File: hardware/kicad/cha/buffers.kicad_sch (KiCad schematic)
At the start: 26 parts, among them U10 74AHCT1G32, U11 74LVC1G07, U3 74LVC16244A, U4 74LVC16244A, U5 74LVC16244A, U6 74LVC16244A, U7 74AHCT16244, U8 74AHCT16244, U9 74AHCT244

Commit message: Circuits imprimés 2 couches : placement et affectation des broches FPGA
- hardware/gen/pcb.py : empreintes et réseaux depuis boards.py, contour
  depuis outline.py ; ancres placées (contacts, rangée de tampons, FPGA,
  mémoires ; CHA : Pico au centre, microSD et bouton en haut), passifs
  au plus près de leur broche, masse coulée sur les deux faces.
- --pins : signaux des FPGA affectés aux broches tournées vers leur
  cible en conservant l'ordre circulaire (pins_opt.json, repris par
  fpga_pins.py) ; stable en trois passes.
- boards.py : canaux des tampons triés selon la position des contacts.
- hardware/gen/route.py : export Specctra, Freerouting, relecture de la
  session, DRC.
Placement-routage FPGA avec les nouvelles broches : en cours de
vérification.

Co-Authored-By: Claude Opus 5.5 <noreply@anthropic.com>
Claude-Session: https://claude.ai/code/session_01WKfXP1YJ8otGxZ5dsY6Agh
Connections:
- net 12M: now also U6.2 (1Y1); no longer U4.19 (4Y1)
- net 2H1: now also U5.23 (4Y4); no longer U4.17 (3Y4)
- net AES_12M: now also U6.47 (1A1); no longer U4.30 (4A1)
- net AES_2H1: now also U5.26 (4A4); no longer U4.32 (3A4)
- net AES_CA4: now also U5.32 (3A4); no longer U4.33 (3A3)
- net AES_DOTA: now also U7.14 (3Y2); no longer U7.13 (3Y1)
- net AES_DOTB: now also U7.13 (3Y1); no longer U7.14 (3Y2)
- net AES_EVEN: now also U5.27 (4A3); no longer U4.29 (4A2)
- net AES_FIXD0: now also U8.3 (1Y2); no longer U7.16 (3Y3)
- net AES_FIXD1: now also U8.2 (1Y1); no longer U7.17 (3Y4)
- net AES_FIXD2: now also U7.23 (4Y4); no longer U7.19 (4Y1)
- net AES_FIXD3: now also U7.22 (4Y3); no longer U7.20 (4Y2)
- net AES_FIXD4: now also U7.20 (4Y2); no longer U7.22 (4Y3)
- net AES_FIXD5: now also U7.19 (4Y1); no longer U7.23 (4Y4)
- net AES_FIXD6: now also U7.17 (3Y4); no longer U8.2 (1Y1)
- net AES_FIXD7: now also U7.16 (3Y3); no longer U8.3 (1Y2)
- net AES_GAD0: now also U7.12 (2Y4); no longer U7.2 (1Y1)
- net AES_GAD1: now also U7.11 (2Y3); no longer U7.3 (1Y2)
- net AES_GAD2: now also U7.9 (2Y2); no longer U7.5 (1Y3)
- net AES_GAD3: now also U7.8 (2Y1); no longer U7.6 (1Y4)
- net AES_GBD0: now also U7.6 (1Y4); no longer U7.8 (2Y1)
- net AES_GBD1: now also U7.5 (1Y3); no longer U7.9 (2Y2)
- net AES_GBD2: now also U7.3 (1Y2); no longer U7.11 (2Y3)
- net AES_GBD3: now also U7.2 (1Y1); no longer U7.12 (2Y4)
- net AES_H: now also U5.29 (4A2); no longer U4.26 (4A4)
- net AES_LOAD: now also U5.30 (4A1); no longer U4.27 (4A3)
- net AES_P0: now also U5.35 (3A2); no longer U3.47 (1A1)
- net AES_P1: now also U5.33 (3A3); no longer U3.46 (1A2)
- net AES_P10: now also U4.26 (4A4); no longer U3.33 (3A3)
- net AES_P11: now also U5.47 (1A1); no longer U3.32 (3A4)
- net AES_P12: now also U4.29 (4A2); no longer U3.30 (4A1)
- net AES_P13: now also U4.27 (4A3); no longer U3.29 (4A2)
- net AES_P14: now also U4.32 (3A4); no longer U3.27 (4A3)
- net AES_P15: now also U4.30 (4A1); no longer U3.26 (4A4)
- net AES_P16: now also U4.35 (3A2); no longer U4.47 (1A1)
- net AES_P17: now also U4.33 (3A3); no longer U4.46 (1A2)
- net AES_P18: now also U4.37 (2A4); no longer U4.44 (1A3)
- net AES_P19: now also U4.36 (3A1); no longer U4.43 (1A4)
- net AES_P2: now also U5.37 (2A4); no longer U3.44 (1A3)
- net AES_P20: now also U4.40 (2A2); no longer U4.41 (2A1)
- net AES_P21: now also U4.38 (2A3); no longer U4.40 (2A2)
- net AES_P22: now also U4.43 (1A4); no longer U4.38 (2A3)
- net AES_P23: now also U4.41 (2A1); no longer U4.37 (2A4)
- net AES_P3: now also U5.36 (3A1); no longer U3.43 (1A4)
- net AES_P4: now also U5.40 (2A2); no longer U3.41 (2A1)
- net AES_P5: now also U5.38 (2A3); no longer U3.40 (2A2)
- net AES_P6: now also U5.43 (1A4); no longer U3.38 (2A3)
- net AES_P7: now also U5.41 (2A1); no longer U3.37 (2A4)
- net AES_P8: now also U5.46 (1A2); no longer U3.36 (3A1)
- net AES_P9: now also U5.44 (1A3); no longer U3.35 (3A2)
- net AES_PCK1B: now also U6.44 (1A3); no longer U4.36 (3A1)
- net AES_PCK2B: now also U6.46 (1A2); no longer U4.35 (3A2)
- net AES_SDA0: now also U4.46 (1A2); no longer U5.47 (1A1)
- net AES_SDA1: now also U4.47 (1A1); no longer U5.46 (1A2)
- net AES_SDA10: now also U3.37 (2A4); no longer U5.33 (3A3)
- net AES_SDA11: now also U3.38 (2A3); no longer U5.32 (3A4)
- net AES_SDA12: now also U3.40 (2A2); no longer U5.30 (4A1)
- net AES_SDA13: now also U3.41 (2A1); no longer U5.29 (4A2)
- net AES_SDA14: now also U3.43 (1A4); no longer U5.27 (4A3)
- net AES_SDA15: now also U3.44 (1A3); no longer U5.26 (4A4)
- net AES_SDA2: now also U3.26 (4A4); no longer U5.44 (1A3)
- net AES_SDA3: now also U3.27 (4A3); no longer U5.43 (1A4)
- net AES_SDA4: now also U3.29 (4A2); no longer U5.41 (2A1)
- net AES_SDA5: now also U3.30 (4A1); no longer U5.40 (2A2)
- net AES_SDA6: now also U3.32 (3A4); no longer U5.38 (2A3)
- net AES_SDA7: now also U3.33 (3A3); no longer U5.37 (2A4)
- net AES_SDA8: now also U3.35 (3A2); no longer U5.36 (3A1)
- net AES_SDA9: now also U3.36 (3A1); no longer U5.35 (3A2)
- net AES_SDMRD: now also U3.46 (1A2); no longer U6.47 (1A1)
- net AES_SDRD0: now also U4.44 (1A3); no longer U6.44 (1A3)
- net AES_SDROM: now also U3.47 (1A1); no longer U6.46 (1A2)
- net CA4: now also U5.17 (3Y4); no longer U4.16 (3Y3)
- net DOTA: now also U7.35 (3A2); no longer U7.36 (3A1)
- net DOTB: now also U7.36 (3A1); no longer U7.35 (3A2)
- net EVEN: now also U5.22 (4Y3); no longer U4.20 (4Y2)
- net FIXD0: now also U8.46 (1A2); no longer U7.33 (3A3)
- net FIXD1: now also U8.47 (1A1); no longer U7.32 (3A4)
- net FIXD2: now also U7.26 (4A4); no longer U7.30 (4A1)
- net FIXD3: now also U7.27 (4A3); no longer U7.29 (4A2)
- net FIXD4: now also U7.29 (4A2); no longer U7.27 (4A3)
- net FIXD5: now also U7.30 (4A1); no longer U7.26 (4A4)
- net FIXD6: now also U7.32 (3A4); no longer U8.47 (1A1)
- net FIXD7: now also U7.33 (3A3); no longer U8.46 (1A2)
- net GAD0: now also U7.37 (2A4); no longer U7.47 (1A1)
- net GAD1: now also U7.38 (2A3); no longer U7.46 (1A2)
- net GAD2: now also U7.40 (2A2); no longer U7.44 (1A3)
- net GAD3: now also U7.41 (2A1); no longer U7.43 (1A4)
- net GBD0: now also U7.43 (1A4); no longer U7.41 (2A1)
- net GBD1: now also U7.44 (1A3); no longer U7.40 (2A2)
- net GBD2: now also U7.46 (1A2); no longer U7.38 (2A3)
- net GBD3: now also U7.47 (1A1); no longer U7.37 (2A4)
- net H: now also U5.20 (4Y2); no longer U4.23 (4Y4)
- net LOAD: now also U5.19 (4Y1); no longer U4.22 (4Y3)
- net P0: now also U5.14 (3Y2); no longer U3.2 (1Y1)
- net P1: now also U5.16 (3Y3); no longer U3.3 (1Y2)
- net P10: now also U4.23 (4Y4); no longer U3.16 (3Y3)
- net P11: now also U5.2 (1Y1); no longer U3.17 (3Y4)
- net P12: now also U4.20 (4Y2); no longer U3.19 (4Y1)
- net P13: now also U4.22 (4Y3); no longer U3.20 (4Y2)
- net P14: now also U4.17 (3Y4); no longer U3.22 (4Y3)
- net P15: now also U4.19 (4Y1); no longer U3.23 (4Y4)
- net P16: now also U4.14 (3Y2); no longer U4.2 (1Y1)
- net P17: now also U4.16 (3Y3); no longer U4.3 (1Y2)
- net P18: now also U4.12 (2Y4); no longer U4.5 (1Y3)
- net P19: now also U4.13 (3Y1); no longer U4.6 (1Y4)
- net P2: now also U5.12 (2Y4); no longer U3.5 (1Y3)
- net P20: now also U4.9 (2Y2); no longer U4.8 (2Y1)
- net P21: now also U4.11 (2Y3); no longer U4.9 (2Y2)
- net P22: now also U4.6 (1Y4); no longer U4.11 (2Y3)
- net P23: now also U4.8 (2Y1); no longer U4.12 (2Y4)
- net P3: now also U5.13 (3Y1); no longer U3.6 (1Y4)
- net P4: now also U5.9 (2Y2); no longer U3.8 (2Y1)
- net P5: now also U5.11 (2Y3); no longer U3.9 (2Y2)
- net P6: now also U5.6 (1Y4); no longer U3.11 (2Y3)
- net P7: now also U5.8 (2Y1); no longer U3.12 (2Y4)
- net P8: now also U5.3 (1Y2); no longer U3.13 (3Y1)
- net P9: now also U5.5 (1Y3); no longer U3.14 (3Y2)
- net PCK1B: now also U6.5 (1Y3); no longer U4.13 (3Y1)
- net PCK2B: now also U6.3 (1Y2); no longer U4.14 (3Y2)
- net SDA0: now also U4.3 (1Y2); no longer U5.2 (1Y1)
- net SDA1: now also U4.2 (1Y1); no longer U5.3 (1Y2)
- net SDA10: now also U3.12 (2Y4); no longer U5.16 (3Y3)
- net SDA11: now also U3.11 (2Y3); no longer U5.17 (3Y4)
- net SDA12: now also U3.9 (2Y2); no longer U5.19 (4Y1)
- net SDA13: now also U3.8 (2Y1); no longer U5.20 (4Y2)
- net SDA14: now also U3.6 (1Y4); no longer U5.22 (4Y3)
- net SDA15: now also U3.5 (1Y3); no longer U5.23 (4Y4)
- net SDA2: now also U3.23 (4Y4); no longer U5.5 (1Y3)
- net SDA3: now also U3.22 (4Y3); no longer U5.6 (1Y4)
- net SDA4: now also U3.20 (4Y2); no longer U5.8 (2Y1)
- net SDA5: now also U3.19 (4Y1); no longer U5.9 (2Y2)
- net SDA6: now also U3.17 (3Y4); no longer U5.11 (2Y3)
- net SDA7: now also U3.16 (3Y3); no longer U5.12 (2Y4)
- net SDA8: now also U3.14 (3Y2); no longer U5.13 (3Y1)
- net SDA9: now also U3.13 (3Y1); no longer U5.14 (3Y2)
- net SDMRD_N: now also U3.3 (1Y2); no longer U6.2 (1Y1)
- net SDRD0_N: now also U4.5 (1Y3); no longer U6.5 (1Y3)
- net SDROM_N: now also U3.2 (1Y1); no longer U6.3 (1Y2)

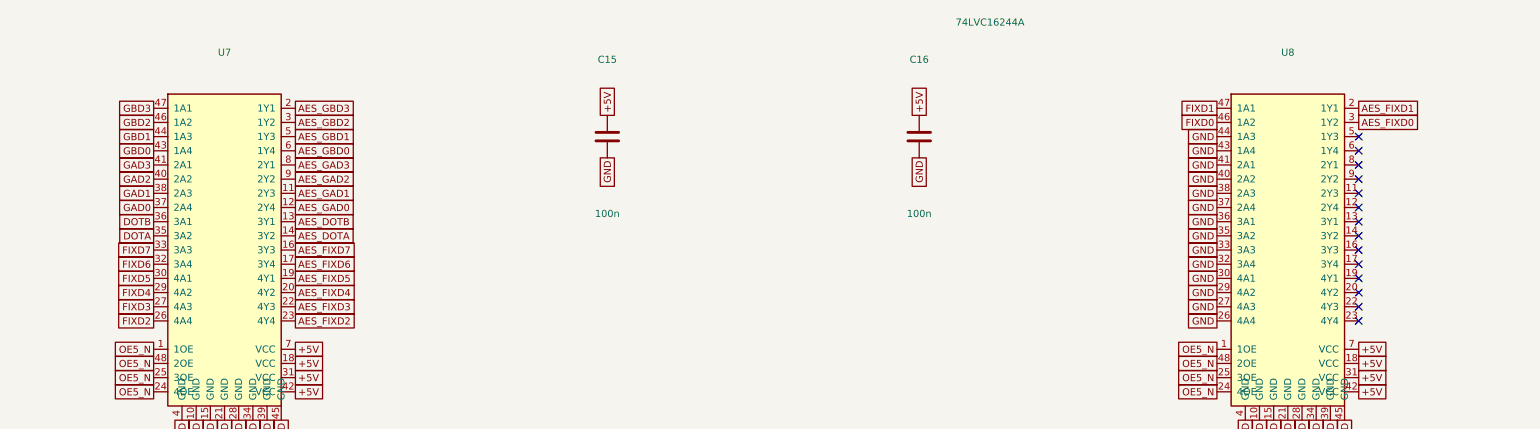
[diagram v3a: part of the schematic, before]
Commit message: CHA : canaux du tampon de sortie U7 groupés par FPGA source
Couche fixe (FPGA SM) puis sprites (FPGA C), chaque groupe dans l'ordre
des contacts : les deux groupes ne se croisent plus le long de la
rangée d'entrée du tampon, où les pistes FIXD enfermaient DOTA et GAD0.
Broches des FPGA C et SM réoptimisées, carte CHA régénérée (contrôle
Freerouting sans violation) ; nouveau routage en cours.

Co-Authored-By: Claude Opus 5.5 <noreply@anthropic.com>
Claude-Session: https://claude.ai/code/session_01WKfXP1YJ8otGxZ5dsY6Agh
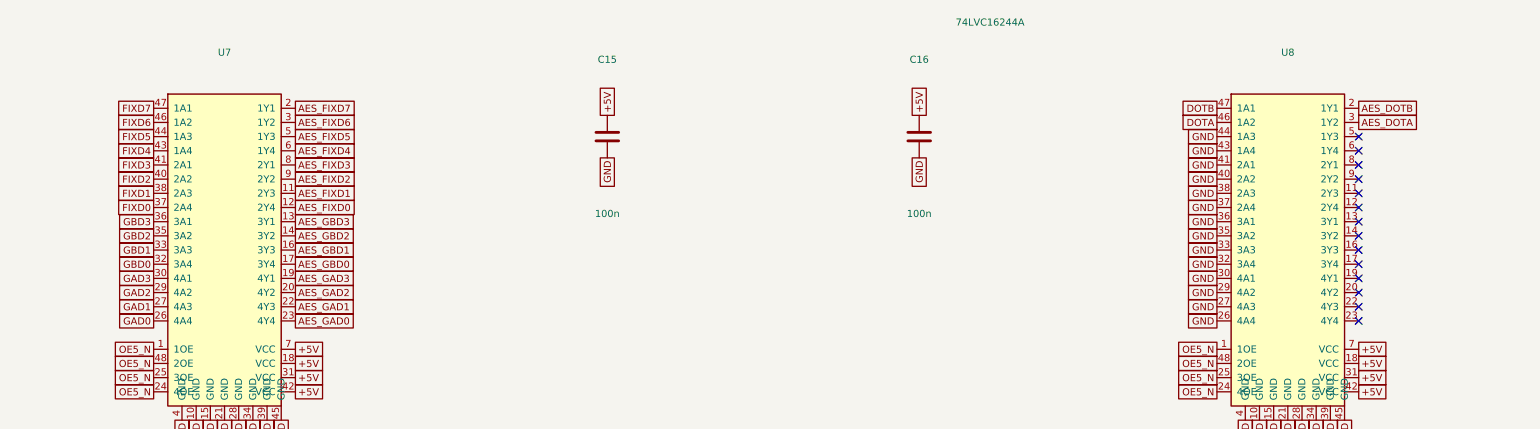
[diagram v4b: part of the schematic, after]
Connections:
- net AES_DOTA: now also U8.3 (1Y2); no longer U7.14 (3Y2)
- net AES_DOTB: now also U8.2 (1Y1); no longer U7.13 (3Y1)
- net AES_FIXD0: now also U7.12 (2Y4); no longer U8.3 (1Y2)
- net AES_FIXD1: now also U7.11 (2Y3); no longer U8.2 (1Y1)
- net AES_FIXD2: now also U7.9 (2Y2); no longer U7.23 (4Y4)
- net AES_FIXD3: now also U7.8 (2Y1); no longer U7.22 (4Y3)
- net AES_FIXD4: now also U7.6 (1Y4); no longer U7.20 (4Y2)
- net AES_FIXD5: now also U7.5 (1Y3); no longer U7.19 (4Y1)
- net AES_FIXD6: now also U7.3 (1Y2); no longer U7.17 (3Y4)
- net AES_FIXD7: now also U7.2 (1Y1); no longer U7.16 (3Y3)
- net AES_GAD0: now also U7.23 (4Y4); no longer U7.12 (2Y4)
- net AES_GAD1: now also U7.22 (4Y3); no longer U7.11 (2Y3)
- net AES_GAD2: now also U7.20 (4Y2); no longer U7.9 (2Y2)
- net AES_GAD3: now also U7.19 (4Y1); no longer U7.8 (2Y1)
- net AES_GBD0: now also U7.17 (3Y4); no longer U7.6 (1Y4)
- net AES_GBD1: now also U7.16 (3Y3); no longer U7.5 (1Y3)
- net AES_GBD2: now also U7.14 (3Y2); no longer U7.3 (1Y2)
- net AES_GBD3: now also U7.13 (3Y1); no longer U7.2 (1Y1)
- net DOTA: now also U8.46 (1A2); no longer U7.35 (3A2)
- net DOTB: now also U8.47 (1A1); no longer U7.36 (3A1)
- net FIXD0: now also U7.37 (2A4); no longer U8.46 (1A2)
- net FIXD1: now also U7.38 (2A3); no longer U8.47 (1A1)
- net FIXD2: now also U7.40 (2A2); no longer U7.26 (4A4)
- net FIXD3: now also U7.41 (2A1); no longer U7.27 (4A3)
- net FIXD4: now also U7.43 (1A4); no longer U7.29 (4A2)
- net FIXD5: now also U7.44 (1A3); no longer U7.30 (4A1)
- net FIXD6: now also U7.46 (1A2); no longer U7.32 (3A4)
- net FIXD7: now also U7.47 (1A1); no longer U7.33 (3A3)
- net GAD0: now also U7.26 (4A4); no longer U7.37 (2A4)
- net GAD1: now also U7.27 (4A3); no longer U7.38 (2A3)
- net GAD2: now also U7.29 (4A2); no longer U7.40 (2A2)
- net GAD3: now also U7.30 (4A1); no longer U7.41 (2A1)
- net GBD0: now also U7.32 (3A4); no longer U7.43 (1A4)
- net GBD1: now also U7.33 (3A3); no longer U7.44 (1A3)
- net GBD2: now also U7.35 (3A2); no longer U7.46 (1A2)
- net GBD3: now also U7.36 (3A1); no longer U7.47 (1A1)

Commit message: Régulateur 3,3 V à découpage, horloge SDRAM adaptée côté FPGA, U8 en 74AHCT125
- AP63203 (TSOT-23-6, sortie fixe 3,3 V, ~90 %) à la place de
  l'AMS1117 : ~0,15 W de pertes au lieu de ~0,75 W et moins de courant
  tiré sur le 5 V de la console ; L 4,7 µH, Cin 10 µF, Cout 2 x 22 µF.
- Résistance série de 33 ohms de l'horloge SDRAM déclarée avec le FPGA :
  placée à 2,7 mm de sa broche (au lieu de ~30 mm, côté SDRAM).
- CHA : U8 (16244 pour 2 canaux) remplacé par un 74AHCT125.
Cartes replacées, contrôle Freerouting sans violation ; routage des
deux cartes et vérification de timing en cours.

Co-Authored-By: Claude Opus 5.5 <noreply@anthropic.com>
Claude-Session: https://claude.ai/code/session_01WKfXP1YJ8otGxZ5dsY6Agh
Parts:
- removed C7, C8: 100n, Capacitor_SMD:C_0603_1608Metric, symbol Device:C
- removed U8: 74AHCT16244, Package_SO:TSSOP-48_6.1x12.5mm_P0.5mm, symbol SDAES:x16244
- added C22: 100n, Capacitor_SMD:C_0603_1608Metric, symbol Device:C
- added U8: 74AHCT125, Package_SO:TSSOP-14_4.4x5mm_P0.65mm, symbol 74xx:74LS125
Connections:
- net +3V3: now also C15.1, C16.1, C22.1; no longer C21.1
- net +5V: now also C21.1, U8.10, U8.13, U8.14 (VCC); no longer C15.1, C16.1
- net AES_DOTA: now also U8.6
- net AES_DOTB: now also U8.3
- net DOTA: now also U8.5
- net DOTB: now also U8.2
- net GND: now also C22.2, U8.12, U8.7 (GND), U8.9
- net OE5_N: now also U8.1, U8.4
- no-connect marks 28 -> 16

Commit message: CHA : canaux des tampons d'entrée groupés par FPGA de destination
SM seul (bus Z80, PCK2B, 2H1) à gauche, bus P0-P15 au milieu, C seul à
droite, chaque groupe dans l'ordre des contacts : le faisceau SDA entre
le FPGA SM et U3 ne se croise plus avec les signaux du FPGA C (SDA4
restait non routable). Carte CHA replacée, broches réoptimisées,
contrôle Freerouting sans violation ; routage en cours.

Co-Authored-By: Claude Opus 5.5 <noreply@anthropic.com>
Claude-Session: https://claude.ai/code/session_01WKfXP1YJ8otGxZ5dsY6Agh
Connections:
- net 12M: now also U6.3 (1Y2); no longer U6.2 (1Y1)
- net 2H1: now also U4.6 (1Y4); no longer U5.23 (4Y4)
- net AES_12M: now also U6.46 (1A2); no longer U6.47 (1A1)
- net AES_2H1: now also U4.43 (1A4); no longer U5.26 (4A4)
- net AES_CA4: now also U5.29 (4A2); no longer U5.32 (3A4)
- net AES_EVEN: now also U6.47 (1A1); no longer U5.27 (4A3)
- net AES_H: now also U5.26 (4A4); no longer U5.29 (4A2)
- net AES_LOAD: now also U5.27 (4A3); no longer U5.30 (4A1)
- net AES_P0: now also U5.43 (1A4); no longer U5.35 (3A2)
- net AES_P1: now also U5.41 (2A1); no longer U5.33 (3A3)
- net AES_P10: now also U4.35 (3A2); no longer U4.26 (4A4)
- net AES_P11: now also U4.33 (3A3); no longer U5.47 (1A1)
- net AES_P12: now also U4.37 (2A4); no longer U4.29 (4A2)
- net AES_P13: now also U4.36 (3A1); no longer U4.27 (4A3)
- net AES_P14: now also U4.40 (2A2); no longer U4.32 (3A4)
- net AES_P15: now also U4.38 (2A3); no longer U4.30 (4A1)
- net AES_P16: now also U5.32 (3A4); no longer U4.35 (3A2)
- net AES_P17: now also U5.30 (4A1); no longer U4.33 (3A3)
- net AES_P18: now also U5.35 (3A2); no longer U4.37 (2A4)
- net AES_P19: now also U5.33 (3A3); no longer U4.36 (3A1)
- net AES_P2: now also U5.46 (1A2); no longer U5.37 (2A4)
- net AES_P20: now also U5.37 (2A4); no longer U4.40 (2A2)
- net AES_P21: now also U5.36 (3A1); no longer U4.38 (2A3)
- net AES_P22: now also U5.40 (2A2); no longer U4.43 (1A4)
- net AES_P23: now also U5.38 (2A3); no longer U4.41 (2A1)
- net AES_P3: now also U5.44 (1A3); no longer U5.36 (3A1)
- net AES_P4: now also U4.26 (4A4); no longer U5.40 (2A2)
- net AES_P5: now also U5.47 (1A1); no longer U5.38 (2A3)
- net AES_P6: now also U4.29 (4A2); no longer U5.43 (1A4)
- net AES_P7: now also U4.27 (4A3); no longer U5.41 (2A1)
- net AES_P8: now also U4.32 (3A4); no longer U5.46 (1A2)
- net AES_P9: now also U4.30 (4A1); no longer U5.44 (1A3)
- net AES_PCK2B: now also U4.41 (2A1); no longer U6.46 (1A2)
- net CA4: now also U5.20 (4Y2); no longer U5.17 (3Y4)
- net EVEN: now also U6.2 (1Y1); no longer U5.22 (4Y3)
- net H: now also U5.23 (4Y4); no longer U5.20 (4Y2)
- net LOAD: now also U5.22 (4Y3); no longer U5.19 (4Y1)
- net P0: now also U5.6 (1Y4); no longer U5.14 (3Y2)
- net P1: now also U5.8 (2Y1); no longer U5.16 (3Y3)
- net P10: now also U4.14 (3Y2); no longer U4.23 (4Y4)
- net P11: now also U4.16 (3Y3); no longer U5.2 (1Y1)
- net P12: now also U4.12 (2Y4); no longer U4.20 (4Y2)
- net P13: now also U4.13 (3Y1); no longer U4.22 (4Y3)
- net P14: now also U4.9 (2Y2); no longer U4.17 (3Y4)
- net P15: now also U4.11 (2Y3); no longer U4.19 (4Y1)
- net P16: now also U5.17 (3Y4); no longer U4.14 (3Y2)
- net P17: now also U5.19 (4Y1); no longer U4.16 (3Y3)
- net P18: now also U5.14 (3Y2); no longer U4.12 (2Y4)
- net P19: now also U5.16 (3Y3); no longer U4.13 (3Y1)
- net P2: now also U5.3 (1Y2); no longer U5.12 (2Y4)
- net P20: now also U5.12 (2Y4); no longer U4.9 (2Y2)
- net P21: now also U5.13 (3Y1); no longer U4.11 (2Y3)
- net P22: now also U5.9 (2Y2); no longer U4.6 (1Y4)
- net P23: now also U5.11 (2Y3); no longer U4.8 (2Y1)
- net P3: now also U5.5 (1Y3); no longer U5.13 (3Y1)
- net P4: now also U4.23 (4Y4); no longer U5.9 (2Y2)
- net P5: now also U5.2 (1Y1); no longer U5.11 (2Y3)
- net P6: now also U4.20 (4Y2); no longer U5.6 (1Y4)
- net P7: now also U4.22 (4Y3); no longer U5.8 (2Y1)
- net P8: now also U4.17 (3Y4); no longer U5.3 (1Y2)
- net P9: now also U4.19 (4Y1); no longer U5.5 (1Y3)
- net PCK2B: now also U4.8 (2Y1); no longer U6.3 (1Y2)
